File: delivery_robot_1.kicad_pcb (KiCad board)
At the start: 4 copper layers, 100 x 100 mm, 159 parts, among them J1 SWD, J10 Port C/D breakout, J13 Pi 5 link, J14 Pi 5 power, J15 Motor2 encoder, J16 MDD20A PWM2/DIR2/GND, J17 Latch servo, J18 AUX1 Notecard, J19 AUX2 LiDAR, J2 XT30PW-M, J20 AUX3 GNSS, J21 AUX4 IMU, J22 AUX force-on, J4 BOOT0 jumper, J5 Power test points, J6 MDD20A PWM1/DIR1/GND, J7 Motor1 encoder, J8 Port A breakout, J9 Port B breakout, Q1 SQJ409EP, Q2 DMN63D8L, SW1 RESET, U1 STM32F091RCTx, U10 74LVC2G17, U2 TPSM63606RDLR, U3 TPS54202DDCR, U4 TPS7A8101DRBR, U5 TPSM63606RDLR, U6 USBLC6-4SC6, U7 USBLC6-4SC6, U8 SN74LVC1T45DBV, U9 74LVC2G17, Y3 8MHz

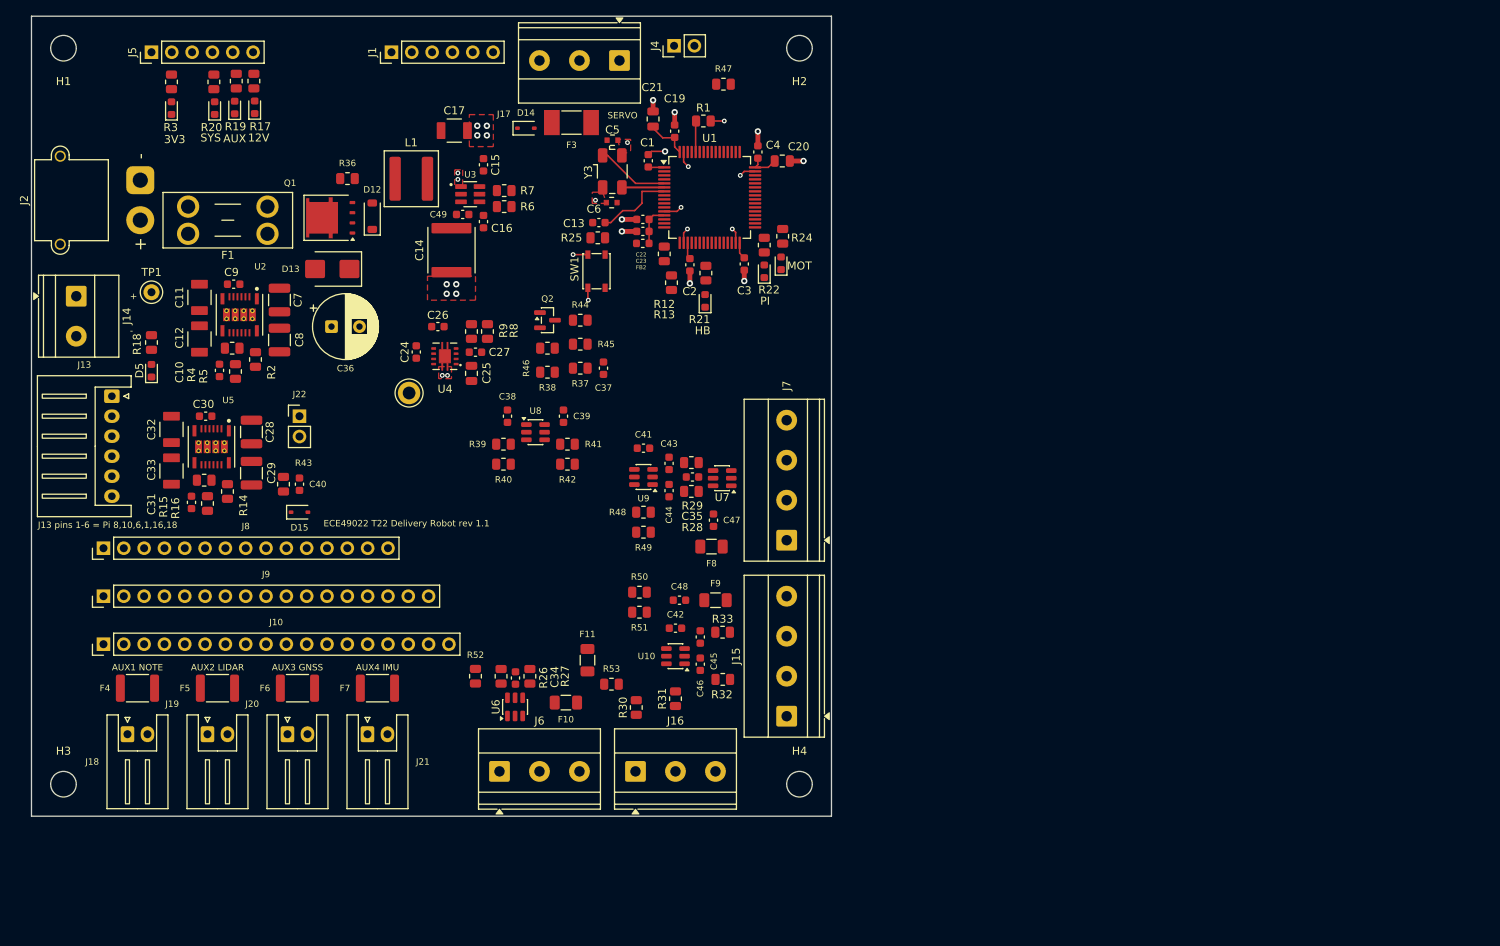
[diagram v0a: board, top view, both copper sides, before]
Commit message: Park the new parts beside the board for manual placement
The 55 footprints added by the design review now sit to the right of the
board outline in nine groups instead of the rough placement, so Venya
can lay them out by hand. Each group has a title on User.Comments
saying where it belongs (input protection, battery sense, U3 HF cap,
Pi link, latch servo, encoder 1, encoder 2, motor driver, AUX ports).

Kept on the board: C36 moved next to the U2/U5 input caps and J8-J10
up 12 mm (these free the spot after F1 and the bottom-left edge for the
new parts), J13's new footprint in its old slot, the LED rail-name
silkscreen, the J14 +/- and J13 pin-map labels and the board name. The
AUX-port and SERVO labels are removed until those parts are placed.

Venya's tracks and vias are unchanged (87, identical). DRC: 0 errors,
3 existing text-size warnings, parity clean.

Co-Authored-By: Claude Opus 5.5 <noreply@anthropic.com>
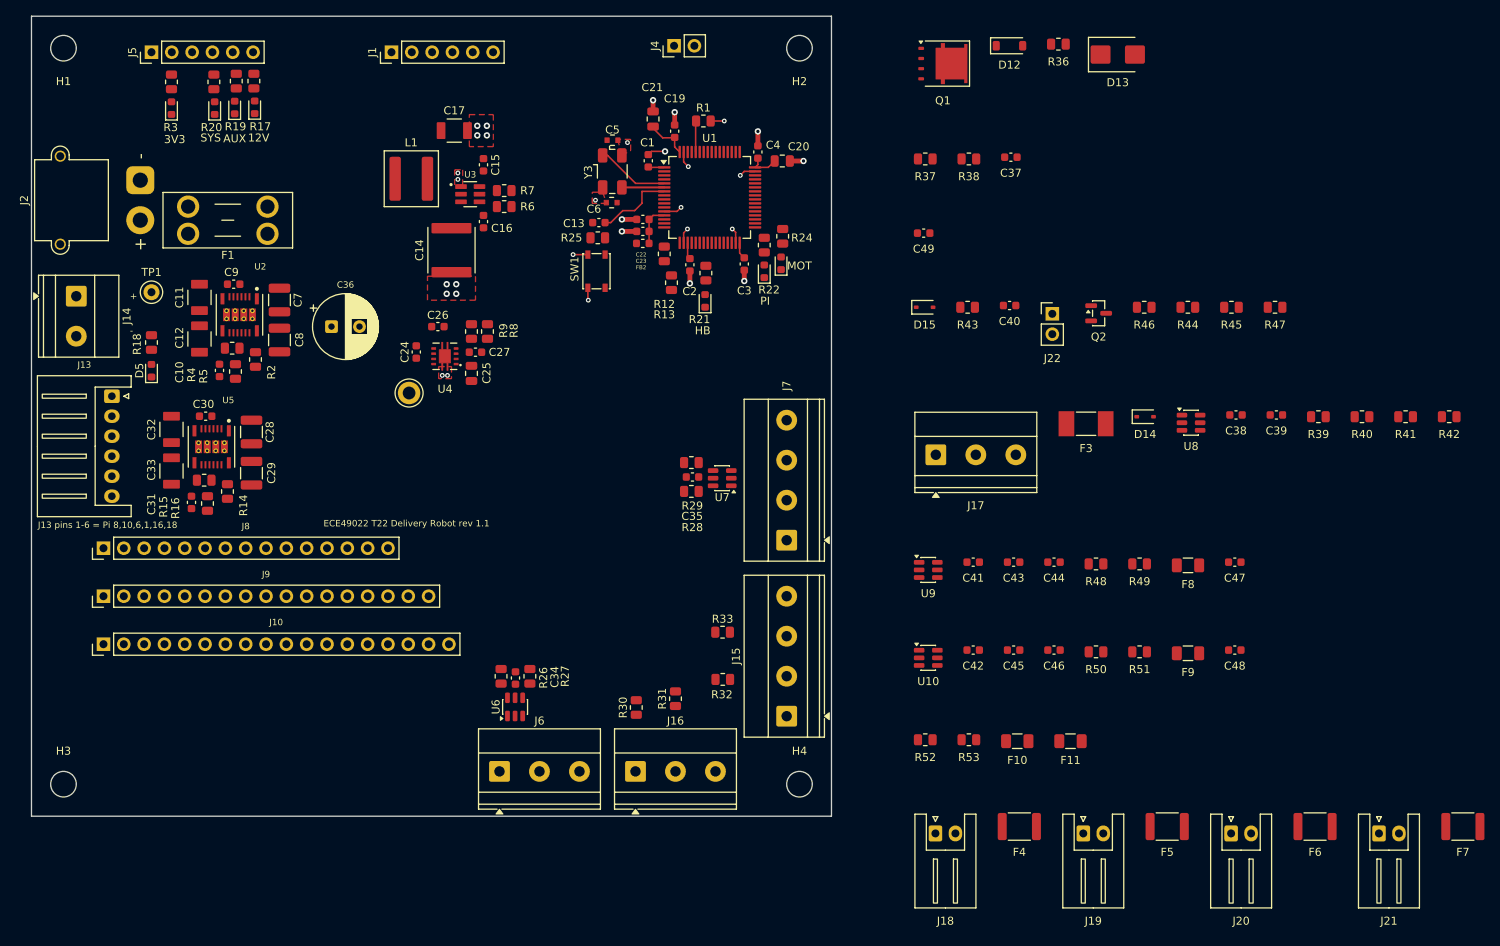
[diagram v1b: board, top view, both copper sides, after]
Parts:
- moved F7 136.8 mm to (263.9, 151.3)
- moved F6 128.4 mm to (245.4, 151.3)
- moved J21 127.0 mm to (253.4, 152.2)
- moved F5 120.0 mm to (227.0, 151.3)
- moved J20 118.6 mm to (235.0, 152.2)
- moved F4 111.6 mm to (208.5, 151.3)
- moved R42 110.4 mm to (262.2, 100.1)
- moved J19 110.2 mm to (216.5, 152.2)
- moved R40 107.5 mm to (251.3, 100.1)
- moved R41 104.8 mm to (256.8, 100.1)
- moved R39 101.9 mm to (245.9, 100.1)
- moved D13 101.8 mm to (220.8, 54.8), turned to 0 degrees
- moved J18 101.8 mm to (198.0, 152.2)
- moved J22 95.0 mm to (212.6, 87.2)
- moved C40 91.5 mm to (207.3, 86.2), turned to 0 degrees
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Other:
- board text added: "AUX ports - J18-J21 on a board edge, PTC F4-F7 at each"
- board text added: "Battery sense - divider near PA0"
- board text added: "Encoder 1 - buffer + RC between R28/R29 and the MCU, PTC/cap at J7"
- board text added: "Encoder 2 - buffer + RC between R32/R33 and the MCU, PTC/cap at J15"
- board text added: "Input protection - after F1 (Q1 tab toward F1; D13 TVS next to C36)"
- board text added: "Latch servo - J17 on a board edge, F3 + D14 at J17, U8 group near PB10/PB11"
- board text added: "Motor driver - R52/R53 PWM pull-downs, F10/F11 in J6/J16 pin-3 ground"
- board text added: "Pi link - AUX enable near U5, reset/BOOT0/sense near the MCU"
- board text added: "U3 HF input cap - at U3 VIN (pin 3) / GND (pin 1)"
- board text removed: "AUX1 NOTE"
- board text removed: "AUX2 LIDAR"
- board text removed: "AUX3 GNSS"
- board text removed: "AUX4 IMU"
- board text removed: "SERVO"
